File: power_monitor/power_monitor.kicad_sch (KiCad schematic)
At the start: 31 parts, among them J1 AVR-ISP-6, J2 Conn_01x06_Female, J3 Conn_01x04_Socket, J4 BATT, J5 VEH, U1 ATmega328-A, U2 ACS712ELCTR-20A, U4 AZ1117-3.3, U5 TS2940CW50, Y1 8M

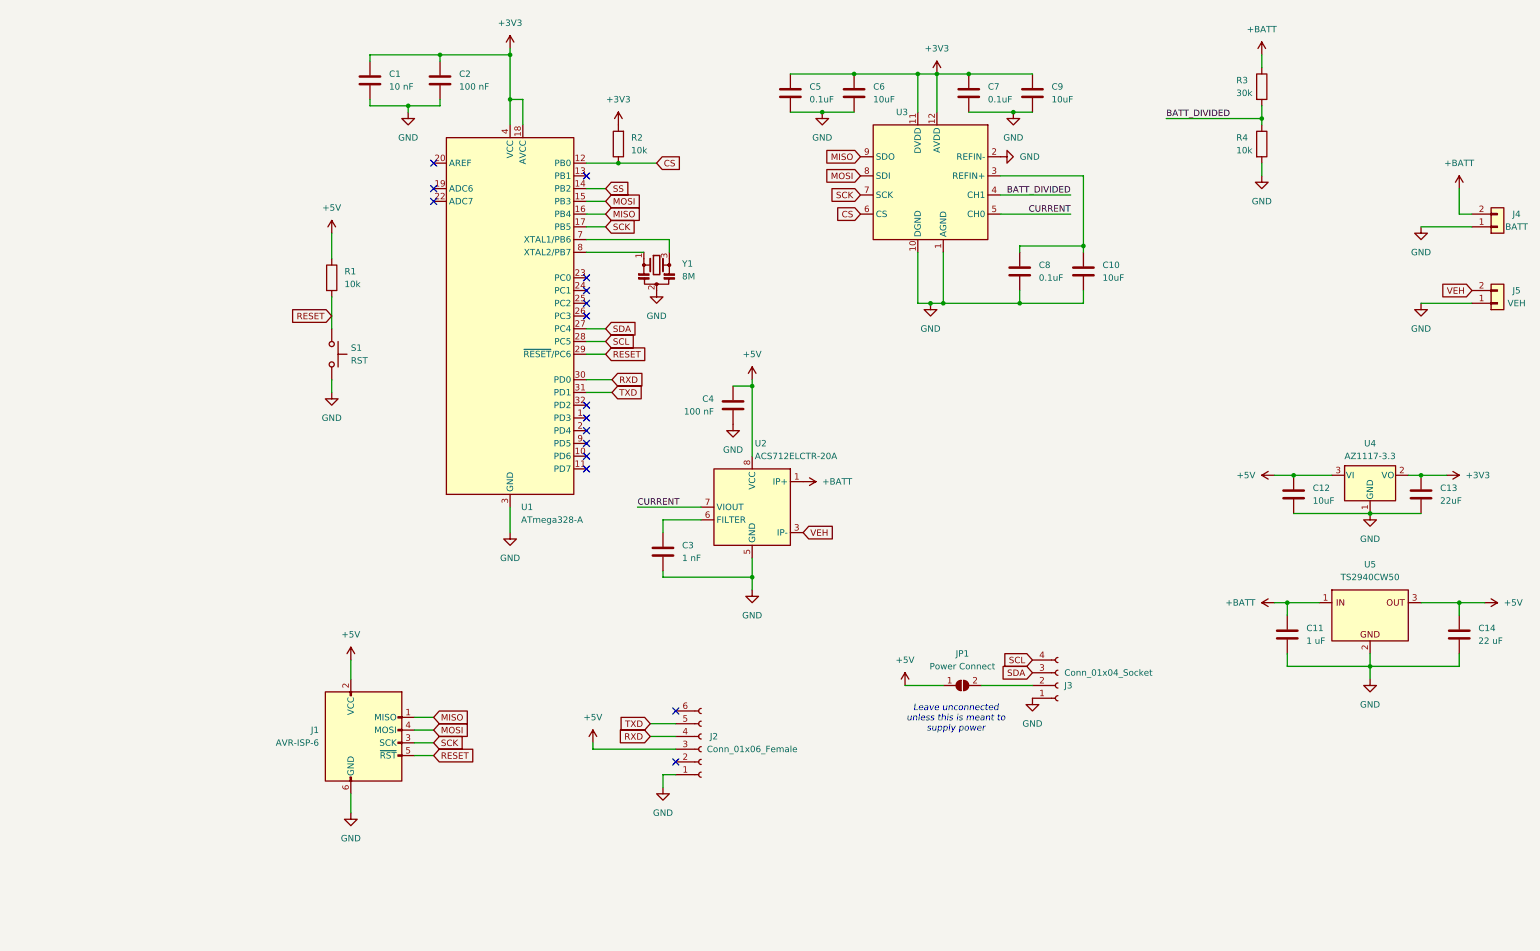
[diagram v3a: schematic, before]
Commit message: PCB Layout
Created initial PCB layout and included more complicated connections to give an idea of what's going on. There's a connection that goes under the board since my brain does not know how to rearrange the components to work all on the front. Also, I made a board outline :D. Also this made me a bit crazy
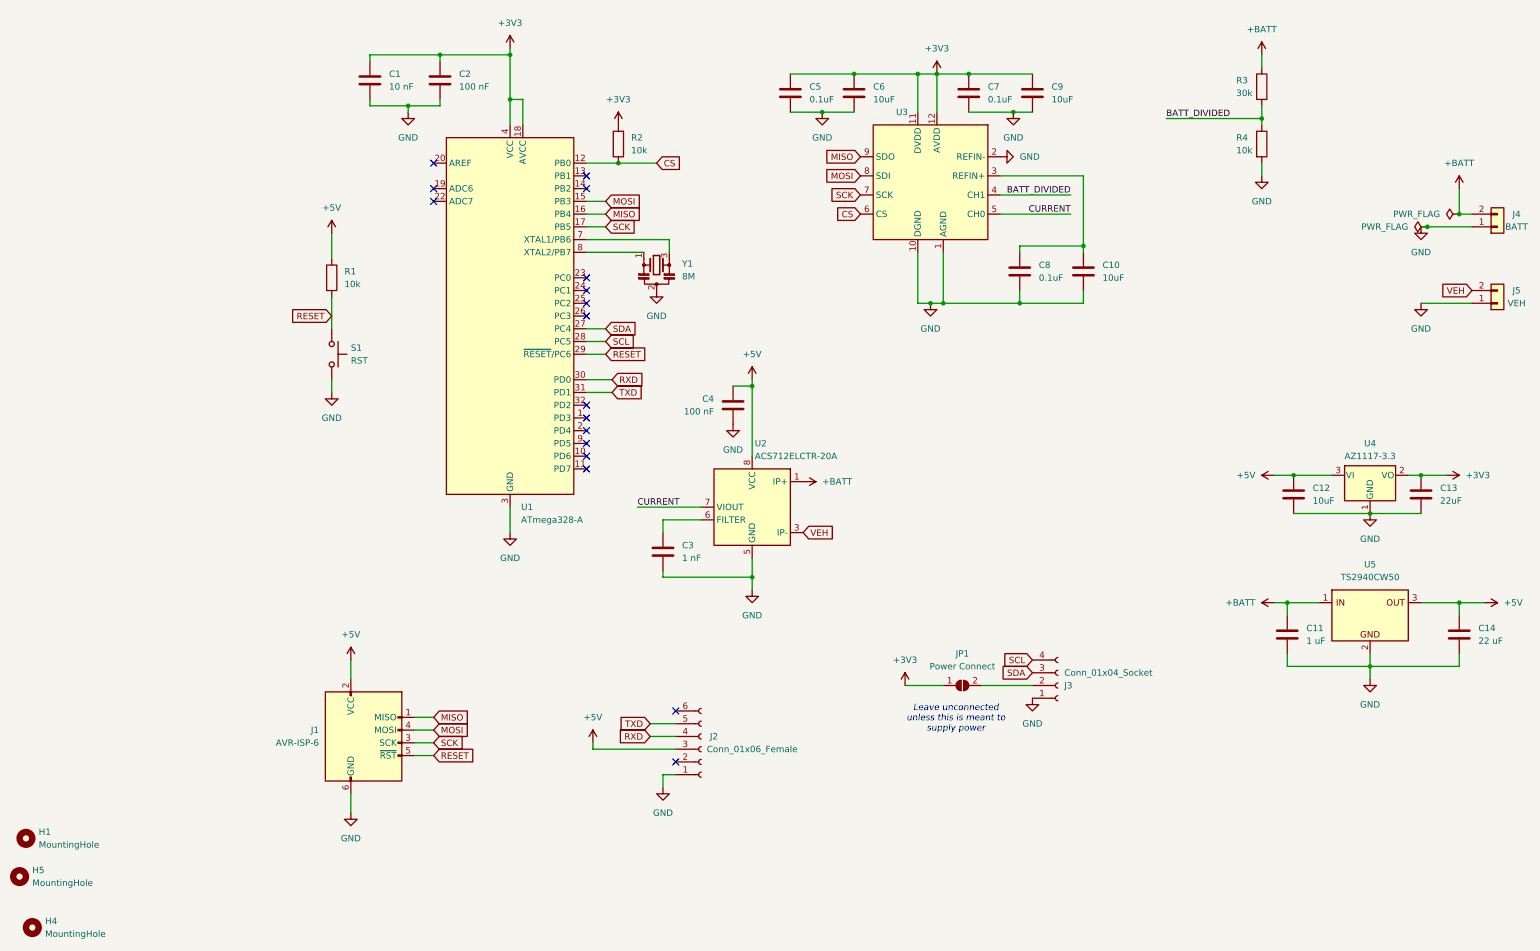
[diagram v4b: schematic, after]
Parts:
- added H1, H4, H5: MountingHole, MountingHole:MountingHole_3.2mm_M3_ISO14580, symbol Mechanical:MountingHole
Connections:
- net +3V3: now also JP1.1 (A)
- net +5V: no longer JP1.1 (A)
- net GND renamed EP
- net EP: now also U3.13 (EP)
- net SS: no longer names the net of U1.14 (PB2)
- no-connect marks 16 -> 17
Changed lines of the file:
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@@
   (junction (at 255.27 138.43) (diameter 0) (color 0 0 0 0)
   )
+  (junction (at 255.27 60.96) (diameter 0) (color 0 0 0 0)
+  )
   (junction (at 66.04 29.21) (diameter 0) (color 0 0 0 0)
   )
@@
   )
   (junction (at 114.3 133.35) (diameter 0) (color 0 0 0 0)
+  )
+  (junction (at 248.92 63.5) (diameter 0) (color 0 0 0 0)
   )
   (junction (at 151.13 33.02) (diameter 0) (color 0 0 0 0)
@@
   (no_connect (at 50.8 50.8))
   (no_connect (at 81.28 78.74))
+  (no_connect (at 81.28 55.88))
   (no_connect (at 81.28 73.66))
   (no_connect (at 50.8 55.88))
@@
     (stroke (width 0) (type default))
   )
-  (wire (pts (xy 247.65 63.5) (xy 257.81 63.5))
+  (wire (pts (xy 247.65 63.5) (xy 248.92 63.5))
     (stroke (width 0) (type default))
   )
@@
     (stroke (width 0) (type default))
   )
-  (wire (pts (xy 81.28 55.88) (xy 85.09 55.88))
-    (stroke (width 0) (type default))
-  )
   (wire (pts (xy 180.34 67.31) (xy 167.64 67.31))
     (stroke (width 0) (type default))
@@
   )
   (wire (pts (xy 157.48 33.02) (xy 170.18 33.02))
+    (stroke (width 0) (type default))
+  )
+  (wire (pts (xy 248.92 63.5) (xy 257.81 63.5))
     (stroke (width 0) (type default))
   )
@@
     (effects (font (size 1.27 1.27)) (justify left))
     (property "Intersheetrefs" "${INTERSHEET_REFS}" (at 92.5226 94.0594 0)
-      (effects (font (size 1.27 1.27)) (justify left) hide)
-    )
-  )
-  (global_label "SS" (shape input) (at 85.09 55.88 0) (fields_autoplaced)
-    (effects (font (size 1.27 1.27)) (justify left))
-    (property "Intersheetrefs" "${INTERSHEET_REFS}" (at 89.9221 55.8006 0)
       (effects (font (size 1.27 1.27)) (justify left) hide)
     )
@@
     )
   )
+  (symbol (lib_id "Mechanical:MountingHole") (at -31.75 193.04 0) (unit 1)
+    (in_bom no) (on_board yes) (dnp no) (fields_autoplaced)
+    (property "Reference" "H5" (at -29.21 191.77 0)
+      (effects (font (size 1.27 1.27)) (justify left))
+    )
+    (property "Value" "MountingHole" (at -29.21 194.31 0)
+      (effects (font (size 1.27 1.27)) (justify left))
+    )
+    (property "Footprint" "MountingHole:MountingHole_3.2mm_M3_ISO14580" (at -31.75 193.04 0)
+      (effects (font (size 1.27 1.27)) hide)
+    )
+    (property "Datasheet" "~" (at -31.75 193.04 0)
+      (effects (font (size 1.27 1.27)) hide)
+    )
+    (instances
+      (project "power_monitor"
+        (path "/4799dcbd-1b9e-4a72-be59-db77c8db3c86"
+          (reference "H5") (unit 1)
+        )
+      )
+    )
+  )
   (symbol (lib_id "power:+5V") (at 260.35 138.43 270) (unit 1)
     (in_bom yes) (on_board yes) (dnp no) (fields_autoplaced)
@@
         (path "/4799dcbd-1b9e-4a72-be59-db77c8db3c86"
           (reference "#PWR033") (unit 1)
+        )
+      )
+    )
+  )
+  (symbol (lib_id "power:+3V3") (at 144.78 154.94 0) (unit 1)
+    (in_bom yes) (on_board yes) (dnp no) (fields_autoplaced)
+    (property "Reference" "#PWR017" (at 144.78 158.75 0)
+      (effects (font (size 1.27 1.27)) hide)
+    )
+    (property "Value" "+3V3" (at 144.78 149.86 0)
+      (effects (font (size 1.27 1.27)))
+    )
+    (property "Footprint" "" (at 144.78 154.94 0)
+      (effects (font (size 1.27 1.27)) hide)
+    )
+    (property "Datasheet" "" (at 144.78 154.94 0)
+      (effects (font (size 1.27 1.27)) hide)
+    )
+    (pin "1")
+    (instances
+      (project "power_monitor"
+        (path "/4799dcbd-1b9e-4a72-be59-db77c8db3c86"
+          (reference "#PWR017") (unit 1)
         )
       )
@@
     )
   )
+  (symbol (lib_id "Mechanical:MountingHole") (at -30.48 185.42 0) (unit 1)
+    (in_bom no) (on_board yes) (dnp no) (fields_autoplaced)
+    (property "Reference" "H1" (at -27.94 184.15 0)
+      (effects (font (size 1.27 1.27)) (justify left))
+    )
+    (property "Value" "MountingHole" (at -27.94 186.69 0)
+      (effects (font (size 1.27 1.27)) (justify left))
+    )
+    (property "Footprint" "MountingHole:MountingHole_3.2mm_M3_ISO14580" (at -30.48 185.42 0)
+      (effects (font (size 1.27 1.27)) hide)
+    )
+    (property "Datasheet" "~" (at -30.48 185.42 0)
+      (effects (font (size 1.27 1.27)) hide)
+    )
+    (instances
+      (project "power_monitor"
+        (path "/4799dcbd-1b9e-4a72-be59-db77c8db3c86"
+          (reference "H1") (unit 1)
+        )
+      )
+    )
+  )
   (symbol (lib_id "power:GND") (at 110.49 102.87 0) (mirror y) (unit 1)
     (in_bom yes) (on_board yes) (dnp no) (fields_autoplaced)
@@
     )
   )
+  (symbol (lib_id "power:PWR_FLAG") (at 248.92 63.5 90) (unit 1)
+    (in_bom yes) (on_board yes) (dnp no) (fields_autoplaced)
+    (property "Reference" "#FLG02" (at 247.015 63.5 0)
+      (effects (font (size 1.27 1.27)) hide)
+    )
+    (property "Value" "PWR_FLAG" (at 245.11 63.5 90)
+      (effects (font (size 1.27 1.27)) (justify left))
+    )
+    (property "Footprint" "" (at 248.92 63.5 0)
+      (effects (font (size 1.27 1.27)) hide)
+    )
+    (property "Datasheet" "~" (at 248.92 63.5 0)
+      (effects (font (size 1.27 1.27)) hide)
+    )
+    (pin "1")
+    (instances
+      (project "power_monitor"
+        (path "/4799dcbd-1b9e-4a72-be59-db77c8db3c86"
+          (reference "#FLG02") (unit 1)
+        )
+      )
+    )
+  )
   (symbol (lib_id "power:GND") (at 215.9 53.34 0) (unit 1)
     (in_bom yes) (on_board yes) (dnp no) (fields_autoplaced)
@@
     )
   )
-  (symbol (lib_id "power:+5V") (at 144.78 154.94 0) (unit 1)
-    (in_bom yes) (on_board yes) (dnp no) (fields_autoplaced)
-    (property "Reference" "#PWR017" (at 144.78 158.75 0)
-      (effects (font (size 1.27 1.27)) hide)
-    )
-    (property "Value" "+5V" (at 144.78 149.86 0)
-      (effects (font (size 1.27 1.27)))
-    )
-    (property "Footprint" "" (at 144.78 154.94 0)
-      (effects (font (size 1.27 1.27)) hide)
-    )
-    (property "Datasheet" "" (at 144.78 154.94 0)
-      (effects (font (size 1.27 1.27)) hide)
-    )
-    (pin "1")
-    (instances
-      (project "power_monitor"
-        (path "/4799dcbd-1b9e-4a72-be59-db77c8db3c86"
-          (reference "#PWR017") (unit 1)
+  (symbol (lib_id "Mechanical:MountingHole") (at -29.21 203.2 0) (unit 1)
+    (in_bom no) (on_board yes) (dnp no) (fields_autoplaced)
+    (property "Reference" "H4" (at -26.67 201.93 0)
+      (effects (font (size 1.27 1.27)) (justify left))
+    )
+    (property "Value" "MountingHole" (at -26.67 204.47 0)
+      (effects (font (size 1.27 1.27)) (justify left))
+    )
+    (property "Footprint" "MountingHole:MountingHole_3.2mm_M3_ISO14580" (at -29.21 203.2 0)
+      (effects (font (size 1.27 1.27)) hide)
+    )
+    (property "Datasheet" "~" (at -29.21 203.2 0)
+      (effects (font (size 1.27 1.27)) hide)
+    )
+    (instances
+      (project "power_monitor"
+        (path "/4799dcbd-1b9e-4a72-be59-db77c8db3c86"
+          (reference "H4") (unit 1)
         )
       )
@@
         (path "/4799dcbd-1b9e-4a72-be59-db77c8db3c86"
           (reference "C10") (unit 1)
+        )
+      )
+    )
+  )
+  (symbol (lib_id "power:PWR_FLAG") (at 255.27 60.96 90) (unit 1)
+    (in_bom yes) (on_board yes) (dnp no) (fields_autoplaced)
+    (property "Reference" "#FLG01" (at 253.365 60.96 0)
+      (effects (font (size 1.27 1.27)) hide)
+    )
+    (property "Value" "PWR_FLAG" (at 251.46 60.96 90)
+      (effects (font (size 1.27 1.27)) (justify left))
+    )
+    (property "Footprint" "" (at 255.27 60.96 0)
+      (effects (font (size 1.27 1.27)) hide)
+    )
+    (property "Datasheet" "~" (at 255.27 60.96 0)
+      (effects (font (size 1.27 1.27)) hide)
+    )
+    (pin "1")
+    (instances
+      (project "power_monitor"
+        (path "/4799dcbd-1b9e-4a72-be59-db77c8db3c86"
+          (reference "#FLG01") (unit 1)
         )
       )
@@
     (pin "11")
     (pin "12")
+    (pin "13")
     (pin "2")
     (pin "3")

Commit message: PCB Layout finished
HAHAHAHAHA IT'S DONE. will commence routing.
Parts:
- added H2: MountingHole, MountingHole:MountingHole_3.2mm_M3_ISO14580, symbol Mechanical:MountingHole
- renumbered H5 to H3
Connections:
- net +3V3: now also J1.2 (VCC), J2.3 (Pin_3)
- net +5V: no longer J1.2 (VCC), J2.3 (Pin_3)
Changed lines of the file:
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@@
   (symbol (lib_id "Mechanical:MountingHole") (at -31.75 193.04 0) (unit 1)
     (in_bom no) (on_board yes) (dnp no) (fields_autoplaced)
-    (property "Reference" "H5" (at -29.21 191.77 0)
+    (property "Reference" "H3" (at -29.21 191.77 0)
       (effects (font (size 1.27 1.27)) (justify left))
     )
@@
       (project "power_monitor"
         (path "/4799dcbd-1b9e-4a72-be59-db77c8db3c86"
-          (reference "H5") (unit 1)
+          (reference "H3") (unit 1)
         )
       )
@@
         (path "/4799dcbd-1b9e-4a72-be59-db77c8db3c86"
           (reference "#PWR017") (unit 1)
-        )
-      )
-    )
-  )
-  (symbol (lib_id "power:+5V") (at 34.29 149.86 0) (unit 1)
-    (in_bom yes) (on_board yes) (dnp no) (fields_autoplaced)
-    (property "Reference" "#PWR03" (at 34.29 153.67 0)
-      (effects (font (size 1.27 1.27)) hide)
-    )
-    (property "Value" "+5V" (at 34.29 144.78 0)
-      (effects (font (size 1.27 1.27)))
-    )
-    (property "Footprint" "" (at 34.29 149.86 0)
-      (effects (font (size 1.27 1.27)) hide)
-    )
-    (property "Datasheet" "" (at 34.29 149.86 0)
-      (effects (font (size 1.27 1.27)) hide)
-    )
-    (pin "1")
-    (instances
-      (project "power_monitor"
-        (path "/4799dcbd-1b9e-4a72-be59-db77c8db3c86"
-          (reference "#PWR03") (unit 1)
         )
       )
@@
     )
   )
+  (symbol (lib_id "power:+3V3") (at 82.55 166.37 0) (unit 1)
+    (in_bom yes) (on_board yes) (dnp no) (fields_autoplaced)
+    (property "Reference" "#PWR03" (at 82.55 170.18 0)
+      (effects (font (size 1.27 1.27)) hide)
+    )
+    (property "Value" "+3V3" (at 82.55 161.29 0)
+      (effects (font (size 1.27 1.27)))
+    )
+    (property "Footprint" "" (at 82.55 166.37 0)
+      (effects (font (size 1.27 1.27)) hide)
+    )
+    (property "Datasheet" "" (at 82.55 166.37 0)
+      (effects (font (size 1.27 1.27)) hide)
+    )
+    (pin "1")
+    (instances
+      (project "power_monitor"
+        (path "/4799dcbd-1b9e-4a72-be59-db77c8db3c86"
+          (reference "#PWR03") (unit 1)
+        )
+      )
+    )
+  )
   (symbol (lib_id "Device:C") (at 96.52 128.27 0) (unit 1)
     (in_bom yes) (on_board yes) (dnp no) (fields_autoplaced)
@@
         (path "/4799dcbd-1b9e-4a72-be59-db77c8db3c86"
           (reference "#PWR019") (unit 1)
+        )
+      )
+    )
+  )
+  (symbol (lib_id "Mechanical:MountingHole") (at -29.21 177.8 0) (unit 1)
+    (in_bom no) (on_board yes) (dnp no) (fields_autoplaced)
+    (property "Reference" "H2" (at -26.67 176.53 0)
+      (effects (font (size 1.27 1.27)) (justify left))
+    )
+    (property "Value" "MountingHole" (at -26.67 179.07 0)
+      (effects (font (size 1.27 1.27)) (justify left))
+    )
+    (property "Footprint" "MountingHole:MountingHole_3.2mm_M3_ISO14580" (at -29.21 177.8 0)
+      (effects (font (size 1.27 1.27)) hide)
+    )
+    (property "Datasheet" "~" (at -29.21 177.8 0)
+      (effects (font (size 1.27 1.27)) hide)
+    )
+    (instances
+      (project "power_monitor"
+        (path "/4799dcbd-1b9e-4a72-be59-db77c8db3c86"
+          (reference "H2") (unit 1)
         )
       )
@@
         (path "/4799dcbd-1b9e-4a72-be59-db77c8db3c86"
           (reference "U2") (unit 1)
-        )
-      )
-    )
-  )
-  (symbol (lib_id "power:+5V") (at 82.55 166.37 0) (unit 1)
-    (in_bom yes) (on_board yes) (dnp no) (fields_autoplaced)
-    (property "Reference" "#PWR08" (at 82.55 170.18 0)
-      (effects (font (size 1.27 1.27)) hide)
-    )
-    (property "Value" "+5V" (at 82.55 161.29 0)
-      (effects (font (size 1.27 1.27)))
-    )
-    (property "Footprint" "" (at 82.55 166.37 0)
-      (effects (font (size 1.27 1.27)) hide)
-    )
-    (property "Datasheet" "" (at 82.55 166.37 0)
-      (effects (font (size 1.27 1.27)) hide)
-    )
-    (pin "1")
-    (instances
-      (project "power_monitor"
-        (path "/4799dcbd-1b9e-4a72-be59-db77c8db3c86"
-          (reference "#PWR08") (unit 1)
         )
       )
@@
         )
       )
+    )
+  )
+  (symbol (lib_id "power:+3V3") (at 34.29 149.86 0) (unit 1)
+    (in_bom yes) (on_board yes) (dnp no) (fields_autoplaced)
+    (property "Reference" "#PWR08" (at 34.29 153.67 0)
+      (effects (font (size 1.27 1.27)) hide)
+    )
+    (property "Value" "+3V3" (at 34.29 144.78 0)
+      (effects (font (size 1.27 1.27)))
+    )
+    (property "Footprint" "" (at 34.29 149.86 0)
+      (effects (font (size 1.27 1.27)) hide)
+    )
+    (property "Datasheet" "" (at 34.29 149.86 0)
+      (effects (font (size 1.27 1.27)) hide)
+    )
+    (pin "1")
+    (instances
+      (project "power_monitor"
+        (path "/4799dcbd-1b9e-4a72-be59-db77c8db3c86"
+          (reference "#PWR08") (unit 1)
+        )
+      )

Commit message: Touched up values for BOMs
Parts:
- C14: value 22 uF -> 22uF
- C2, C4: value 100 nF -> 0.1uF
- J2, JP1: now left out of the parts list
- U3: value ~ -> MCP3465
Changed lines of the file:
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@@
   (symbol (lib_id "Device:C") (at 52.07 34.29 0) (unit 1)
     (in_bom yes) (on_board yes) (dnp no) (fields_autoplaced)
-    (property "Reference" "C2" (at 55.88 33.0199 0)
-      (effects (font (size 1.27 1.27)) (justify left))
-    )
-    (property "Value" "100 nF" (at 55.88 35.5599 0)
+    (property "Reference" "C2" (at 55.88 33.02 0)
+      (effects (font (size 1.27 1.27)) (justify left))
+    )
+    (property "Value" "0.1uF" (at 55.88 35.56 0)
       (effects (font (size 1.27 1.27)) (justify left))
     )
@@
       (effects (font (size 1.27 1.27)) (justify left))
     )
-    (property "Value" "~" (at 156.21 40.64 0)
+    (property "Value" "MCP3465" (at 156.21 40.64 0)
       (effects (font (size 1.27 1.27)))
     )
@@
   )
   (symbol (lib_id "Connector:Conn_01x06_Female") (at 104.14 167.64 0) (mirror x) (unit 1)
-    (in_bom yes) (on_board yes) (dnp no)
+    (in_bom no) (on_board yes) (dnp no)
     (property "Reference" "J2" (at 106.68 165.1 0)
       (effects (font (size 1.27 1.27)))
@@
   )
   (symbol (lib_id "Jumper:SolderJumper_2_Open") (at 156.21 154.94 0) (unit 1)
-    (in_bom yes) (on_board yes) (dnp no) (fields_autoplaced)
+    (in_bom no) (on_board yes) (dnp no) (fields_autoplaced)
     (property "Reference" "JP1" (at 156.21 148.59 0)
       (effects (font (size 1.27 1.27)))
@@
   (symbol (lib_id "Device:C") (at 255.27 144.78 0) (unit 1)
     (in_bom yes) (on_board yes) (dnp no) (fields_autoplaced)
-    (property "Reference" "C14" (at 259.08 143.5099 0)
-      (effects (font (size 1.27 1.27)) (justify left))
-    )
-    (property "Value" "22 uF" (at 259.08 146.0499 0)
+    (property "Reference" "C14" (at 259.08 143.51 0)
+      (effects (font (size 1.27 1.27)) (justify left))
+    )
+    (property "Value" "22uF" (at 259.08 146.05 0)
       (effects (font (size 1.27 1.27)) (justify left))
     )
@@
   (symbol (lib_id "Device:C") (at 110.49 99.06 0) (mirror y) (unit 1)
     (in_bom yes) (on_board yes) (dnp no) (fields_autoplaced)
-    (property "Reference" "C4" (at 106.68 97.79 0)
-      (effects (font (size 1.27 1.27)) (justify left))
-    )
-    (property "Value" "100 nF" (at 106.68 100.33 0)
-      (effects (font (size 1.27 1.27)) (justify left))
+    (property "Reference" "C4" (at 114.3 97.79 0)
+      (effects (font (size 1.27 1.27)) (justify right))
+    )
+    (property "Value" "0.1uF" (at 114.3 100.33 0)
+      (effects (font (size 1.27 1.27)) (justify right))
     )
     (property "Footprint" "Capacitor_SMD:C_0603_1608Metric" (at 109.5248 102.87 0)
